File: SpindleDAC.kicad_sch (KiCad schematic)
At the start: 10 parts, among them J23 Spindle Out, U16 LTV-817S, U17 ${SIM.PARAMS}, U18 TL431DBZ, U19 ${SIM.PARAMS}

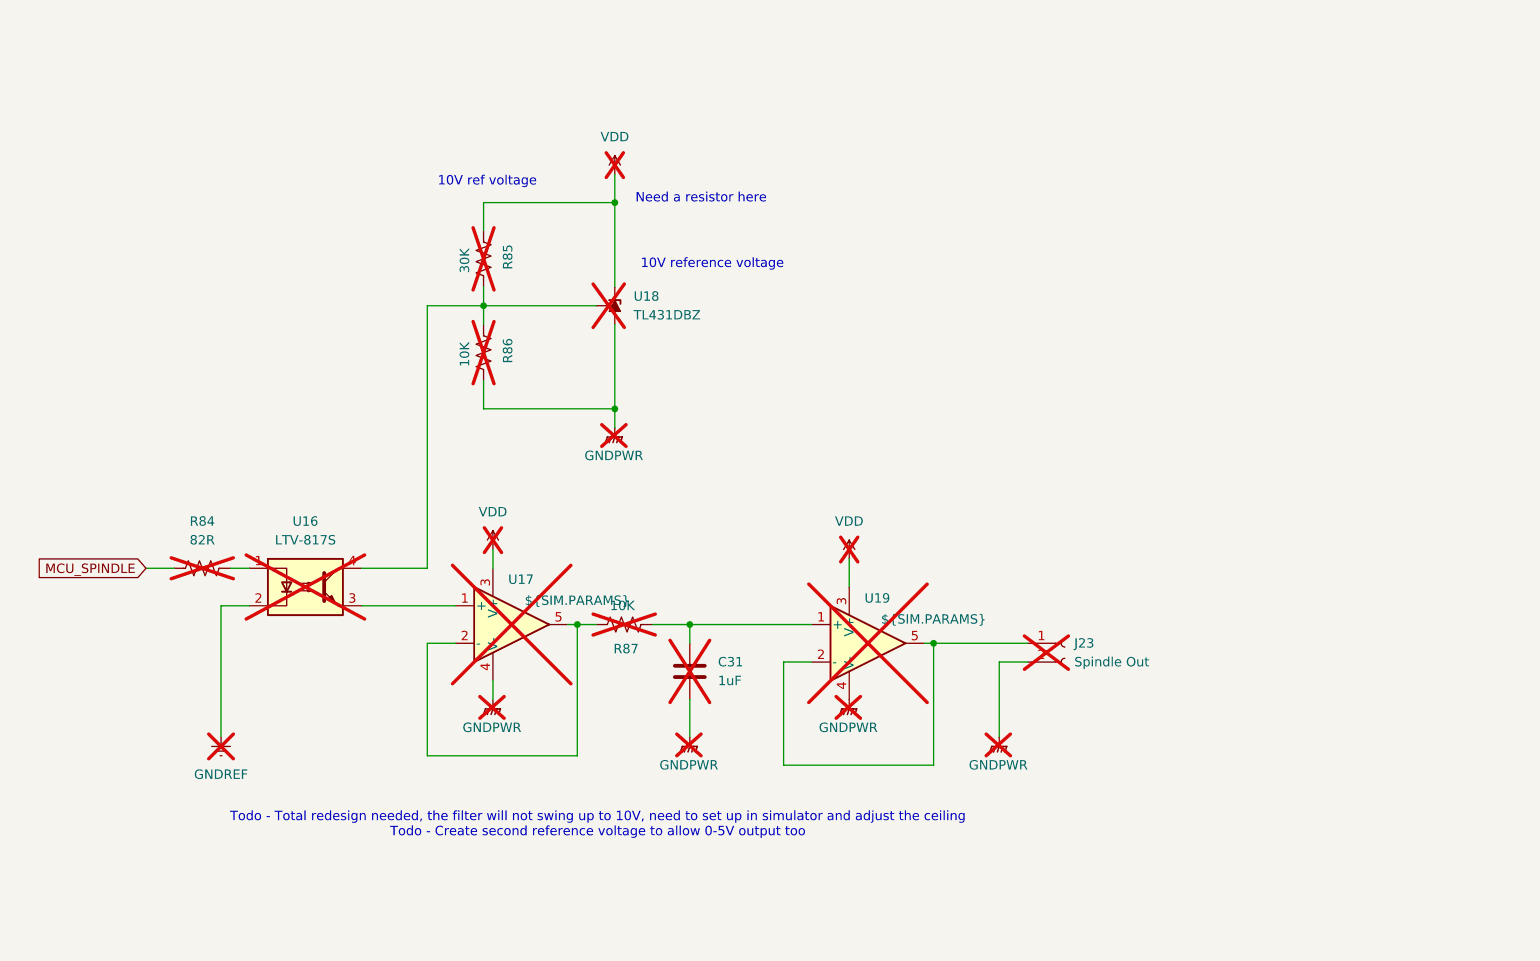
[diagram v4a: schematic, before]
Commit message: Finalised Spindle DAC, working as expected
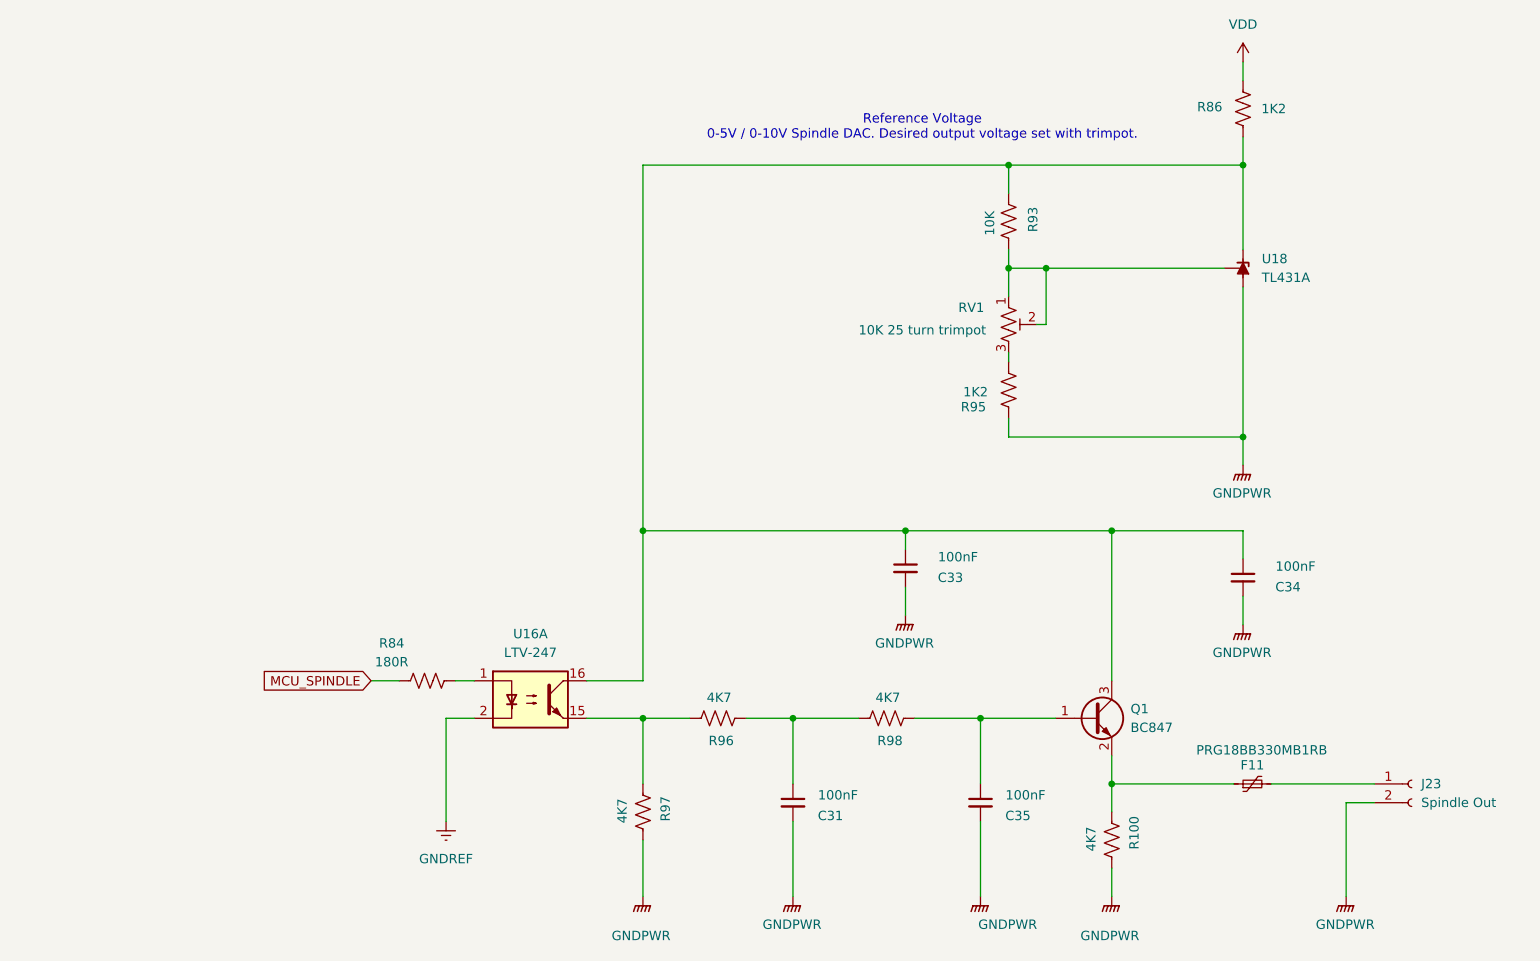
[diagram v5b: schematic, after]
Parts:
- removed C31: 1uF, symbol Device:C
- removed R85: 30K, Resistor_SMD:R_1206_3216Metric_Pad1.30x1.75mm_HandSolder, symbol Device:R_US
- removed R87: 10K, Resistor_SMD:R_1206_3216Metric_Pad1.30x1.75mm_HandSolder, symbol Device:R_US
- removed U16: LTV-817S, Package_SO:SOIC-16_3.9x9.9mm_P1.27mm, symbol Isolator:LTV-817S
- removed U17, U19: ${SIM.PARAMS}, symbol Simulation_SPICE:OPAMP
- added C31, C33, C34, C35: 100nF, Capacitor_SMD:C_1206_3216Metric_Pad1.33x1.80mm_HandSolder, symbol Device:C_Small
- added F11: PRG18BB330MB1RB, Fuse:Fuse_0603_1608Metric_Pad1.05x0.95mm_HandSolder, symbol Device:Polyfuse_Small
- added Q1: BC847, Package_TO_SOT_SMD:SOT-23, symbol Transistor_BJT:BC847
- added R100, R96, R97, R98: 4K7, Resistor_SMD:R_1206_3216Metric_Pad1.30x1.75mm_HandSolder, symbol Device:R_US
- added R93: 10K, Resistor_SMD:R_1206_3216Metric_Pad1.30x1.75mm_HandSolder, symbol Device:R_US
- added R95: 1K2, Resistor_SMD:R_1206_3216Metric_Pad1.30x1.75mm_HandSolder, symbol Device:R_US
- added RV1: 10K 25 turn trimpot, Potentiometer_THT:Potentiometer_Bourns_3266Y_Vertical, symbol Device:R_Potentiometer_Trim_US
- added U16: LTV-247, Package_SO:SOP-16_4.4x10.4mm_P1.27mm, symbol Isolator:LTV-247
- J23: Digikey Part Number (none) -> 1818-QT02ADP83V0000G-ND; Digikey URL (none) -> https://www.digikey.com.au/en/products/detail/amphenol-anyt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; now fitted
- R84: value 82R -> 180R; Digikey Part Number (none) -> 311-180FRCT-ND; Digikey URL (none) -> https://www.digikey.com.au/en/products/detail/yageo/RC1206F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; now fitted
- R86: value 10K -> 1K2; Digikey Part Number 311-10.0KFRCT-ND -> RMCF1206JT1K20CT-ND; Digikey URL https://www.digikey.com.au/en/products/detail/yageo/RC1206F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 -> https://www.digikey.com.au/en/products/detail/stackpole-ele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; now fitted
- U18: value TL431DBZ -> TL431A; Digikey Part Number (none) -> 4878-MMTL431ACT-ND; Digikey URL (none) -> https://www.digikey.com/en/products/detail/diotec-semicondu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; now fitted
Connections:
- net GNDPWR: now also C31.2, C33.2, C34.2, C35.2, R100.2, R95.1, R97.2; no longer R86.2
- net GNDREF: now also U16.2
- net VDD: now also R86.2; no longer U18.1 (K)
- net at J23.1 (Pin_1): now also F11.2
- net at R86.1, U18.2 (K): now also C33.1, C34.1, Q1.3 (C), R93.1, U16.16
- net at R84.2: now also U16.1
- new net: C35.1, Q1.1 (B), R98.1
- new net: C31.1, R96.1, R98.2
- new net: R96.2, R97.1, U16.15
- new net: R95.2, RV1.3
- new net: R93.2, RV1.1, RV1.2, U18.1 (REF)
- new net: F11.1, Q1.2 (E), R100.1
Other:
- note added: "Reference Voltage 0-5V / 0-10V Spindle DAC. Desired output voltage set with trimpot."
- note removed: "10V ref voltage"
- note removed: "10V reference voltage"
- note removed: "Need a resistor here"
- note removed: "Todo - Total redesign needed, the filter will not swing up to 10V, need to set up in simulator and adjust the ceiling Todo - Create second reference voltage to allow 0-5V output too"

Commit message: Added high speed encoder input circuitry. General tidy and updates to readme
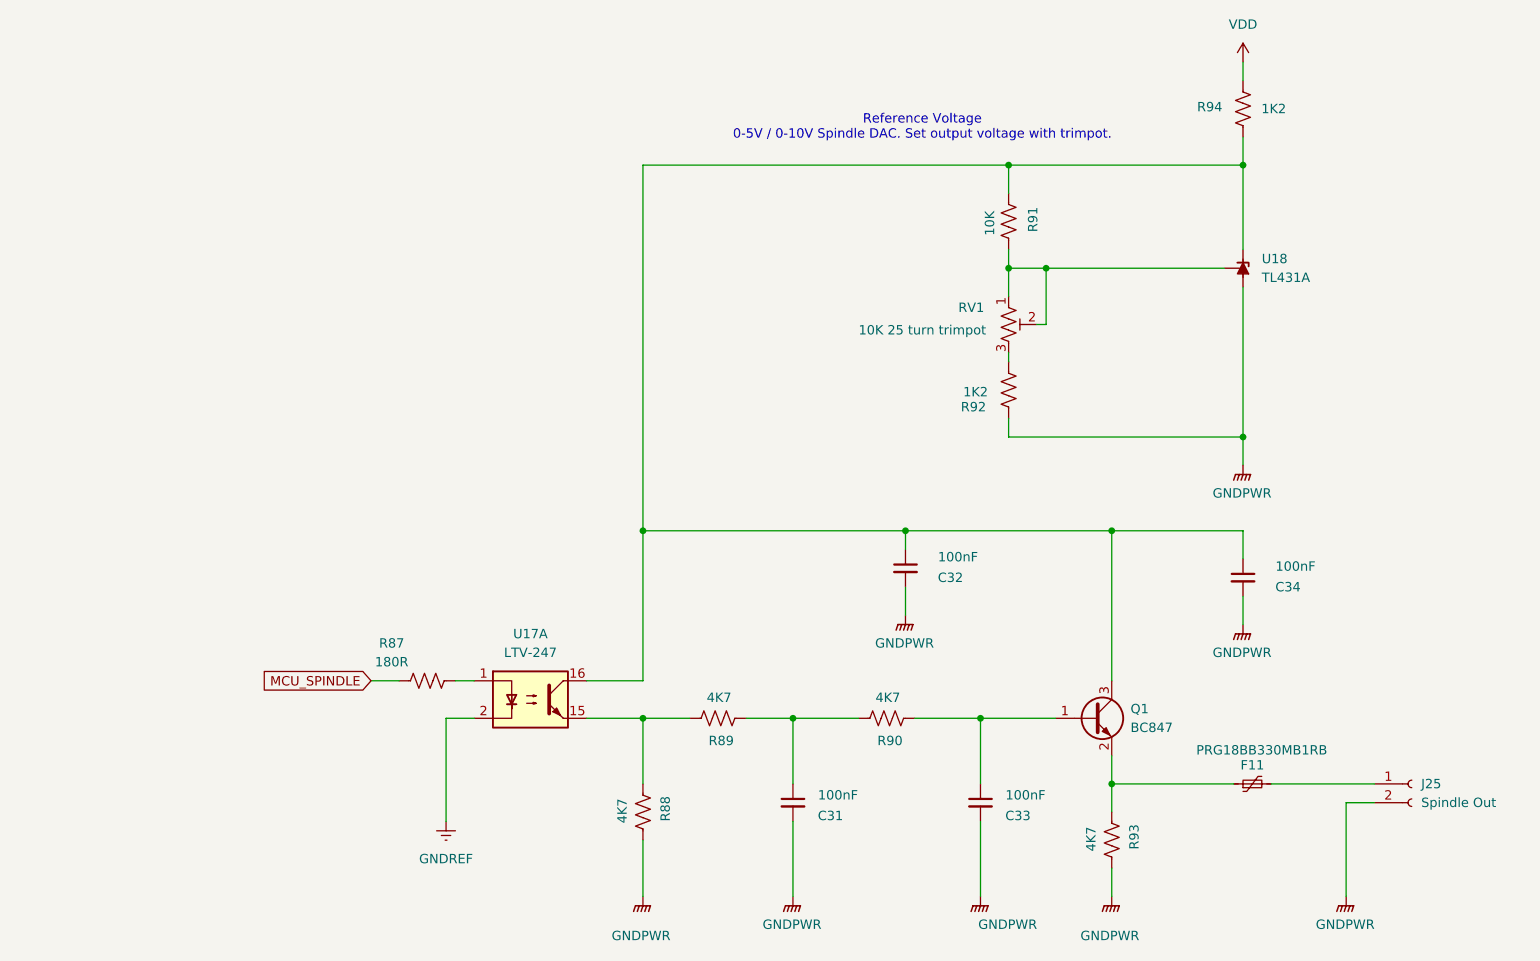
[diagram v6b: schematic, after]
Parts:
- renumbered C33 to C32, C35 to C33, J23 to J25, R84 to R87, R97 to R88, R96 to R89, R98 to R90, R93 to R91, R95 to R92, R100 to R93, R86 to R94, U16 to U17
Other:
- note added: "Reference Voltage 0-5V / 0-10V Spindle DAC. Set output voltage with trimpot."
- note removed: "Reference Voltage 0-5V / 0-10V Spindle DAC. Desired output voltage set with trimpot."

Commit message: Layout for stepper drivers and digital inputs
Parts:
- renumbered C31 to C34, C32 to C35, C33 to C36, C34 to C37
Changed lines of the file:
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@@
 		(on_board yes)
 		(dnp no)
-		(property "Reference" "#PWR0212"
+		(property "Reference" "#PWR0215"
 			(at 189.23 143.51 0)
 			(effects
@@
 			(project "Remora Nucleo F446ZE Hat"
 				(path "/5473abc6-7b93-43cc-a401-f691c4d7d7cf/5cdad347-c6ad-4791-9d53-e4d1ad999196"
-					(reference "#PWR0212")
+					(reference "#PWR0215")
 					(unit 1)
 				)
@@
 		(on_board yes)
 		(dnp no)
-		(property "Reference" "C32"
+		(property "Reference" "C35"
 			(at 167.386 95.25 0)
 			(effects
@@
 			(project "Remora Nucleo F446ZE Hat"
 				(path "/5473abc6-7b93-43cc-a401-f691c4d7d7cf/5cdad347-c6ad-4791-9d53-e4d1ad999196"
-					(reference "C32")
+					(reference "C35")
 					(unit 1)
 				)
@@
 		(dnp no)
 		(fields_autoplaced yes)
-		(property "Reference" "#PWR0207"
+		(property "Reference" "#PWR0210"
 			(at 99.06 134.62 0)
 			(effects
@@
 			(project "Remora Nucleo F446ZE Hat"
 				(path "/5473abc6-7b93-43cc-a401-f691c4d7d7cf/5cdad347-c6ad-4791-9d53-e4d1ad999196"
-					(reference "#PWR0207")
+					(reference "#PWR0210")
 					(unit 1)
 				)
@@
 		(on_board yes)
 		(dnp no)
-		(property "Reference" "C33"
+		(property "Reference" "C36"
 			(at 176.53 127.508 0)
 			(effects
@@
 			(project "Remora Nucleo F446ZE Hat"
 				(path "/5473abc6-7b93-43cc-a401-f691c4d7d7cf/5cdad347-c6ad-4791-9d53-e4d1ad999196"
-					(reference "C33")
+					(reference "C36")
 					(unit 1)
 				)
@@
 		(dnp no)
 		(fields_autoplaced yes)
-		(property "Reference" "#PWR0213"
+		(property "Reference" "#PWR0216"
 			(at 207.01 29.21 0)
 			(effects
@@
 			(project "Remora Nucleo F446ZE Hat"
 				(path "/5473abc6-7b93-43cc-a401-f691c4d7d7cf/5cdad347-c6ad-4791-9d53-e4d1ad999196"
-					(reference "#PWR0213")
+					(reference "#PWR0216")
 					(unit 1)
 				)
@@
 		(dnp no)
 		(fields_autoplaced yes)
-		(property "Reference" "#PWR0210"
+		(property "Reference" "#PWR0213"
 			(at 161.29 105.41 0)
 			(effects
@@
 			(project "Remora Nucleo F446ZE Hat"
 				(path "/5473abc6-7b93-43cc-a401-f691c4d7d7cf/5cdad347-c6ad-4791-9d53-e4d1ad999196"
-					(reference "#PWR0210")
+					(reference "#PWR0213")
 					(unit 1)
 				)
@@
 		(dnp no)
 		(fields_autoplaced yes)
-		(property "Reference" "#PWR0215"
+		(property "Reference" "#PWR0218"
 			(at 207.01 106.68 0)
 			(effects
@@
 			(project "Remora Nucleo F446ZE Hat"
 				(path "/5473abc6-7b93-43cc-a401-f691c4d7d7cf/5cdad347-c6ad-4791-9d53-e4d1ad999196"
-					(reference "#PWR0215")
+					(reference "#PWR0218")
 					(unit 1)
 				)
@@
 		(on_board yes)
 		(dnp no)
-		(property "Reference" "#PWR0208"
+		(property "Reference" "#PWR0211"
 			(at 125.73 143.51 0)
 			(effects
@@
 			(project "Remora Nucleo F446ZE Hat"
 				(path "/5473abc6-7b93-43cc-a401-f691c4d7d7cf/5cdad347-c6ad-4791-9d53-e4d1ad999196"
-					(reference "#PWR0208")
+					(reference "#PWR0211")
 					(unit 1)
 				)
@@
 		(dnp no)
 		(fields_autoplaced yes)
-		(property "Reference" "#PWR0216"
+		(property "Reference" "#PWR0219"
 			(at 220.98 143.51 0)
 			(effects
@@
 			(project "Remora Nucleo F446ZE Hat"
 				(path "/5473abc6-7b93-43cc-a401-f691c4d7d7cf/5cdad347-c6ad-4791-9d53-e4d1ad999196"
-					(reference "#PWR0216")
+					(reference "#PWR0219")
 					(unit 1)
 				)
@@
 		(on_board yes)
 		(dnp no)
-		(property "Reference" "C34"
+		(property "Reference" "C37"
 			(at 213.106 96.52 0)
 			(effects
@@
 			(project "Remora Nucleo F446ZE Hat"
 				(path "/5473abc6-7b93-43cc-a401-f691c4d7d7cf/5cdad347-c6ad-4791-9d53-e4d1ad999196"
-					(reference "C34")
+					(reference "C37")
 					(unit 1)
 				)
@@
 		(dnp no)
 		(fields_autoplaced yes)
-		(property "Reference" "#PWR0214"
+		(property "Reference" "#PWR0217"
 			(at 207.01 85.09 0)
 			(effects
@@
 			(project "Remora Nucleo F446ZE Hat"
 				(path "/5473abc6-7b93-43cc-a401-f691c4d7d7cf/5cdad347-c6ad-4791-9d53-e4d1ad999196"
-					(reference "#PWR0214")
+					(reference "#PWR0217")
 					(unit 1)
 				)
@@
 		(dnp no)
 		(fields_autoplaced yes)
-		(property "Reference" "#PWR0209"
+		(property "Reference" "#PWR0212"
 			(at 146.05 143.51 0)
 			(effects
@@
 			(project "Remora Nucleo F446ZE Hat"
 				(path "/5473abc6-7b93-43cc-a401-f691c4d7d7cf/5cdad347-c6ad-4791-9d53-e4d1ad999196"
-					(reference "#PWR0209")
+					(reference "#PWR0212")
 					(unit 1)
 				)
@@
 		(on_board yes)
 		(dnp no)
-		(property "Reference" "C31"
+		(property "Reference" "C34"
 			(at 151.13 127.508 0)
 			(effects
@@
 			(project "Remora Nucleo F446ZE Hat"
 				(path "/5473abc6-7b93-43cc-a401-f691c4d7d7cf/5cdad347-c6ad-4791-9d53-e4d1ad999196"
-					(reference "C31")
+					(reference "C34")
 					(unit 1)
 				)
@@
 		(on_board yes)
 		(dnp no)
-		(property "Reference" "#PWR0211"
+		(property "Reference" "#PWR0214"
 			(at 171.45 143.51 0)
 			(effects
@@
 			(project "Remora Nucleo F446ZE Hat"
 				(path "/5473abc6-7b93-43cc-a401-f691c4d7d7cf/5cdad347-c6ad-4791-9d53-e4d1ad999196"
-					(reference "#PWR0211")
-					(unit 1)
-				)
+					(reference "#PWR0214")
+					(unit 1)
+				)
